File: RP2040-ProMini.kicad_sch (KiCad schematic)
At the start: 34 parts, among them J1 CONN_L, J2 CONN_U, J3 CONN_R2, J4 CONN_R, Q1 AO3400A, U1 W25Q128JVS, U2 RP2040, U3 MIC5205-3.3YM5, U4 W25Q128JVEIQ, Y1 12MHz

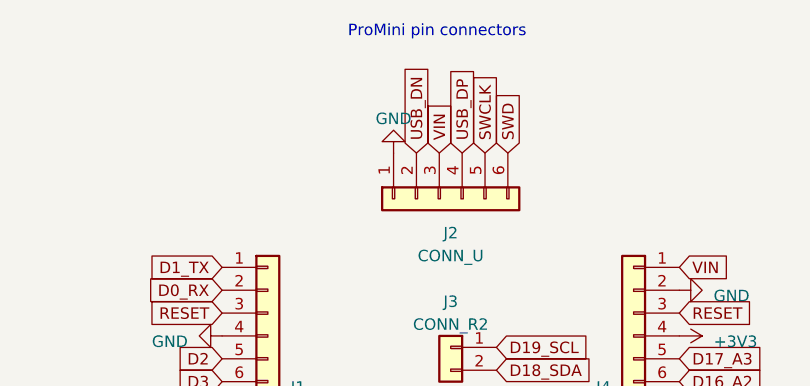
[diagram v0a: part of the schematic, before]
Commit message: Switched D- and GND on debug connector. Added missing VIN text.
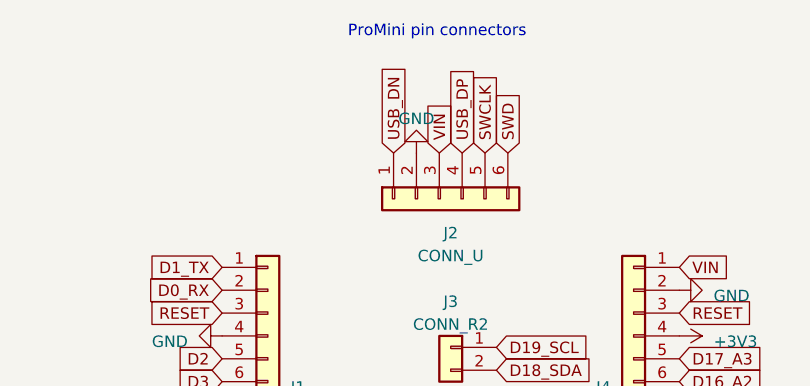
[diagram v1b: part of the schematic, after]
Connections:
- net GND: now also J2.2 (Pin_2); no longer J2.1 (Pin_1)
- net USB_DN: now also J2.1 (Pin_1); no longer J2.2 (Pin_2)
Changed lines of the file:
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@@
   (title_block
     (title "RP2040-ProMini-0010")
-    (date "2023-06-13")
+    (date "2023-06-22")
     (rev "1.0")
     (company "(c) 2023 Andriy Golovnya")
@@
     )
   )
-  (global_label "USB_DN" (shape input) (at 224.79 43.18 90) (fields_autoplaced)
-    (effects (font (size 1.27 1.27)) (justify left))
-    (property "Intersheetrefs" "${INTERSHEET_REFS}" (at 224.79 32.8961 90)
+  (global_label "USB_DN" (shape input) (at 222.25 43.18 90) (fields_autoplaced)
+    (effects (font (size 1.27 1.27)) (justify left))
+    (property "Intersheetrefs" "${INTERSHEET_REFS}" (at 222.25 32.8961 90)
       (effects (font (size 1.27 1.27)) (justify left) hide)
     )
@@
     )
   )
-  (symbol (lib_id "power:GND") (at 222.25 43.18 180) (unit 1)
-    (in_bom yes) (on_board yes) (dnp no) (fields_autoplaced)
-    (property "Reference" "#PWR037" (at 222.25 36.83 0)
-      (effects (font (size 1.27 1.27)) hide)
-    )
-    (property "Value" "GND" (at 222.25 39.37 0)
-      (effects (font (size 1.27 1.27)))
-    )
-    (property "Footprint" "" (at 222.25 43.18 0)
-      (effects (font (size 1.27 1.27)) hide)
-    )
-    (property "Datasheet" "" (at 222.25 43.18 0)
-      (effects (font (size 1.27 1.27)) hide)
-    )
+  (symbol (lib_id "power:GND") (at 224.79 43.18 180) (unit 1)
+    (in_bom yes) (on_board yes) (dnp no) (fields_autoplaced)
+    (property "Reference" "#PWR037" (at 224.79 36.83 0)
+      (effects (font (size 1.27 1.27)) hide)
+    )
+    (property "Value" "GND" (at 224.79 39.37 0)
+      (effects (font (size 1.27 1.27)))
+    )
+    (property "Footprint" "" (at 224.79 43.18 0)
+      (effects (font (size 1.27 1.27)) hide)
+    )
+    (property "Datasheet" "" (at 224.79 43.18 0)
+      (effects (font (size 1.27 1.27)) hide)
+    )

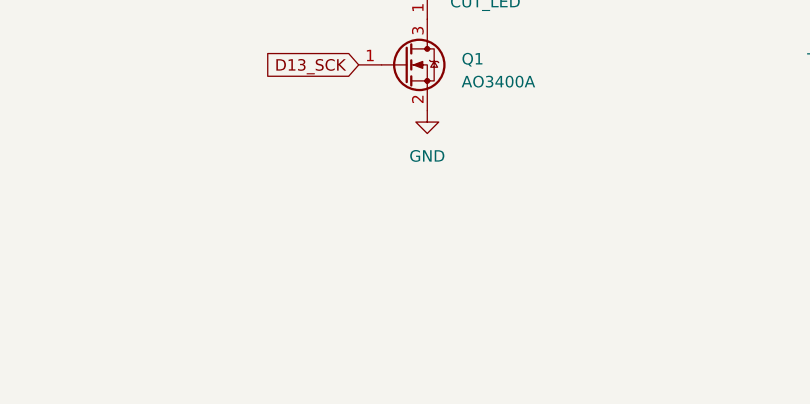
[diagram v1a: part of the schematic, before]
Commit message: Added BOOTSEL button for user convenience
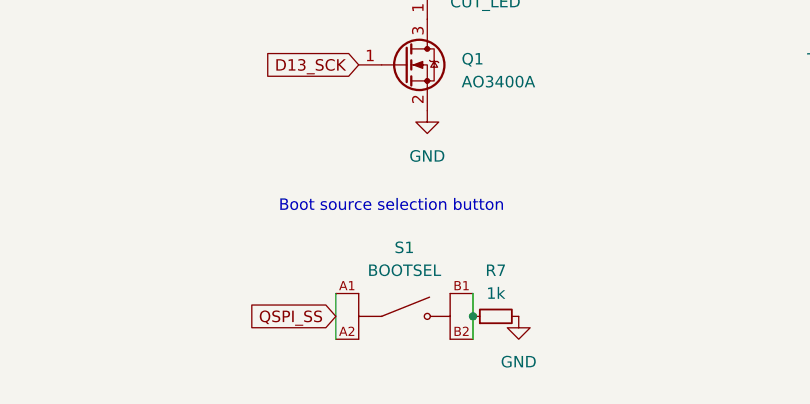
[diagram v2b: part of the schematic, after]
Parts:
- added R7: 1k, Resistor_SMD:R_0402_1005Metric, symbol Device:R_Small
- added S1: BOOTSEL, RP2040-ProMini:SW_EVPBB0AAB000, symbol EVPBB0AAB000:EVPBB0AAB000
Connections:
- net GND: now also R7.2
- net QSPI_SS: now also S1.A1, S1.A2
- new net: R7.1, S1.B1, S1.B2
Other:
- note added: "Boot source selection button"
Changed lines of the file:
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@@
   (title_block
     (title "RP2040-ProMini-0010")
-    (date "2023-06-22")
+    (date "2023-07-04")
     (rev "1.0")
     (company "(c) 2023 Andriy Golovnya")
@@
   )
   (junction (at 255.27 129.54) (diameter 0) (color 0 0 0 0)
+  )
+  (junction (at 72.39 171.45) (diameter 0) (color 0 0 0 0)
   )
   (junction (at 146.05 39.37) (diameter 0) (color 0 0 0 0)
@@
     (stroke (width 0) (type default))
   )
+  (wire (pts (xy 57.15 168.91) (xy 57.15 173.99))
+    (stroke (width 0) (type default))
+  )
   (wire (pts (xy 135.89 39.37) (xy 138.43 39.37))
     (stroke (width 0) (type default))
@@
     (stroke (width 0) (type default))
   )
+  (wire (pts (xy 72.39 171.45) (xy 72.39 173.99))
+    (stroke (width 0) (type default))
+  )
+  (wire (pts (xy 72.39 168.91) (xy 72.39 171.45))
+    (stroke (width 0) (type default))
+  )
   (wire (pts (xy 251.46 129.54) (xy 255.27 129.54))
     (stroke (width 0) (type default))
@@
     (effects (font (size 1.27 1.27)) (justify left bottom))
   )
+  (text "Boot source selection button" (at 50.8 160.02 0)
+    (effects (font (size 1.27 1.27)) (justify left bottom))
+  )
   (text "LDO power supply" (at 220.98 120.65 0)
     (effects (font (size 1.27 1.27)) (justify left bottom))
@@
     )
   )
+  (global_label "QSPI_SS" (shape input) (at 57.15 171.45 180) (fields_autoplaced)
+    (effects (font (size 1.27 1.27)) (justify right))
+    (property "Intersheetrefs" "${INTERSHEET_REFS}" (at 46.4428 171.45 0)
+      (effects (font (size 1.27 1.27)) (justify right) hide)
+    )
+  )
   (global_label "SWCLK" (shape input) (at 208.28 101.6 270) (fields_autoplaced)
     (effects (font (size 1.27 1.27)) (justify right))
@@
     )
   )
+  (symbol (lib_id "EVPBB0AAB000:EVPBB0AAB000") (at 64.77 171.45 0) (unit 1)
+    (in_bom yes) (on_board yes) (dnp no) (fields_autoplaced)
+    (property "Reference" "S1" (at 64.77 163.83 0)
+      (effects (font (size 1.27 1.27)))
+    )
+    (property "Value" "BOOTSEL" (at 64.77 166.37 0)
+      (effects (font (size 1.27 1.27)))
+    )
+    (property "Footprint" "RP2040-ProMini:SW_EVPBB0AAB000" (at 64.77 171.45 0)
+      (effects (font (size 1.27 1.27)) (justify bottom) hide)
+    )
+    (property "Datasheet" "" (at 64.77 171.45 0)
+      (effects (font (size 1.27 1.27)) hide)
+    )
+    (property "ARROW_ELECTRONICS-PURCHASE-URL" "https://snapeda.com/shop?store=Arrow+Electronics&id=584571" (at 64.77 171.45 0)
+      (effects (font (size 1.27 1.27)) (justify bottom) hide)
+    )
+    (property "MOUSER-PURCHASE-URL" "https://snapeda.com/shop?store=Mouser&id=584571" (at 64.77 171.45 0)
+      (effects (font (size 1.27 1.27)) (justify bottom) hide)
+    )
+    (property "MAXIMUM_PACKAGE_HEIGHT" "0.58mm" (at 64.77 171.45 0)
+      (effects (font (size 1.27 1.27)) (justify bottom) hide)
+    )
+    (property "PACKAGE" "None" (at 64.77 171.45 0)
+      (effects (font (size 1.27 1.27)) (justify bottom) hide)
+    )
+    (property "MF" "Panasonic Electronic" (at 64.77 171.45 0)
+      (effects (font (size 1.27 1.27)) (justify bottom) hide)
+    )
+    (property "MP" "EVPBB0AAB000" (at 64.77 171.45 0)
+      (effects (font (size 1.27 1.27)) (justify bottom) hide)
+    )
+    (property "DIGIKEY-PURCHASE-URL" "https://snapeda.com/shop?store=DigiKey&id=584571" (at 64.77 171.45 0)
+      (effects (font (size 1.27 1.27)) (justify bottom) hide)
+    )
+    (property "DIGI-KEY_PART_NUMBER" "P19888CT-ND" (at 64.77 171.45 0)
+      (effects (font (size 1.27 1.27)) (justify bottom) hide)
+    )
+    (property "DESCRIPTION" "Tactile Switch SPST-NO Top Actuated Surface Mount" (at 64.77 171.45 0)
+      (effects (font (size 1.27 1.27)) (justify bottom) hide)
+    )
+    (pin "A1")
+    (pin "A2")
+    (pin "B1")
+    (pin "B2")
+    (instances
+      (project "RP2040-ProMini"
+        (path "/9a38a81c-7302-494f-9784-2ab4342a0a1d"
+          (reference "S1") (unit 1)
+        )
+      )
+    )
+  )
   (symbol (lib_id "Device:C_Small") (at 248.92 99.06 0) (unit 1)
     (in_bom yes) (on_board yes) (dnp no) (fields_autoplaced)
@@
         (path "/9a38a81c-7302-494f-9784-2ab4342a0a1d"
           (reference "#PWR09") (unit 1)
+        )
+      )
+    )
+  )
+  (symbol (lib_id "power:GND") (at 77.47 171.45 0) (unit 1)
+    (in_bom yes) (on_board yes) (dnp no) (fields_autoplaced)
+    (property "Reference" "#PWR049" (at 77.47 177.8 0)
+      (effects (font (size 1.27 1.27)) hide)
+    )
+    (property "Value" "GND" (at 77.47 176.53 0)
+      (effects (font (size 1.27 1.27)))
+    )
+    (property "Footprint" "" (at 77.47 171.45 0)
+      (effects (font (size 1.27 1.27)) hide)
+    )
+    (property "Datasheet" "" (at 77.47 171.45 0)
+      (effects (font (size 1.27 1.27)) hide)
+    )
+    (pin "1")
+    (instances
+      (project "RP2040-ProMini"
+        (path "/9a38a81c-7302-494f-9784-2ab4342a0a1d"
+          (reference "#PWR049") (unit 1)
         )
       )
@@
         )
       )
+    )
+  )
+  (symbol (lib_id "Device:R_Small") (at 74.93 171.45 90) (unit 1)
+    (in_bom yes) (on_board yes) (dnp no) (fields_autoplaced)
+    (property "Reference" "R7" (at 74.93 166.37 90)
+      (effects (font (size 1.27 1.27)))
+    )
+    (property "Value" "1k" (at 74.93 168.91 90)
+      (effects (font (size 1.27 1.27)))
+    )
+    (property "Footprint" "Resistor_SMD:R_0402_1005Metric" (at 74.93 171.45 0)
+      (effects (font (size 1.27 1.27)) hide)
+    )
+    (property "Datasheet" "~" (at 74.93 171.45 0)
+      (effects (font (size 1.27 1.27)) hide)
+    )
+    (pin "1")
+    (pin "2")
+    (instances
+      (project "RP2040-ProMini"
+        (path "/9a38a81c-7302-494f-9784-2ab4342a0a1d"
+          (reference "R7") (unit 1)
+        )
+      )

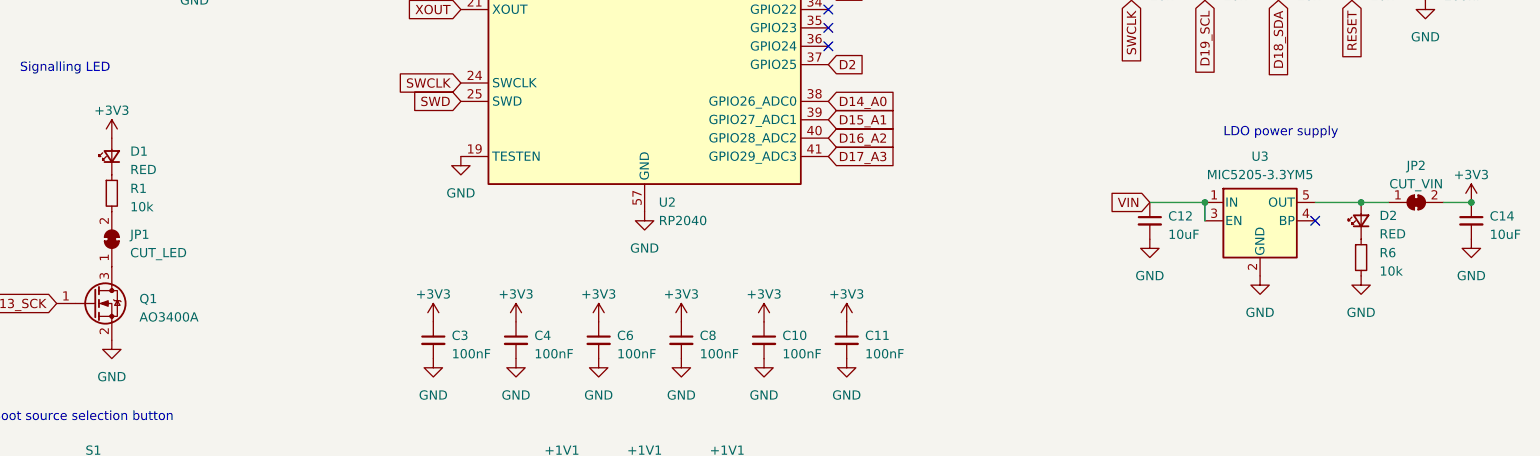
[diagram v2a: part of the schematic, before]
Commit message: Spin off v1.1 to reflect new BOOTSEL button.
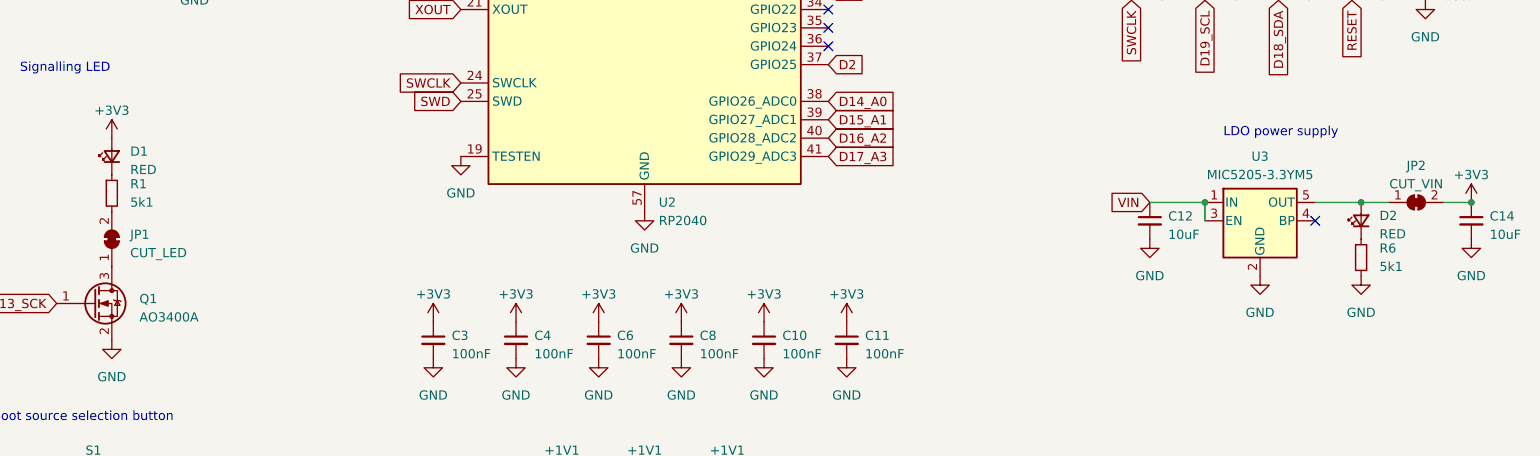
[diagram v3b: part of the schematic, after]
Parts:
- R1, R6: value 10k -> 5k1
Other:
- title: RP2040-ProMini-0010 -> RP2040-ProMini-0011
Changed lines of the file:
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@@
   (paper "A4")
   (title_block
-    (title "RP2040-ProMini-0010")
-    (date "2023-07-04")
-    (rev "1.0")
+    (title "RP2040-ProMini-0011")
+    (date "2023-07-05")
+    (rev "1.1")
     (company "(c) 2023 Andriy Golovnya")
     (comment 1 "RP2040 based board with Arduino Pro Mini footprint")
@@
   (symbol (lib_id "Device:R_Small") (at 67.31 128.27 0) (unit 1)
     (in_bom yes) (on_board yes) (dnp no) (fields_autoplaced)
-    (property "Reference" "R1" (at 69.85 127.635 0)
-      (effects (font (size 1.27 1.27)) (justify left))
-    )
-    (property "Value" "10k" (at 69.85 130.175 0)
+    (property "Reference" "R1" (at 69.85 127 0)
+      (effects (font (size 1.27 1.27)) (justify left))
+    )
+    (property "Value" "5k1" (at 69.85 129.54 0)
       (effects (font (size 1.27 1.27)) (justify left))
     )
@@
   (symbol (lib_id "Device:R_Small") (at 240.03 137.16 0) (unit 1)
     (in_bom yes) (on_board yes) (dnp no) (fields_autoplaced)
-    (property "Reference" "R6" (at 242.57 136.525 0)
-      (effects (font (size 1.27 1.27)) (justify left))
-    )
-    (property "Value" "10k" (at 242.57 139.065 0)
-      (effects (font (size 1.27 1.27)) (justify left))
-    )
+    (property "Reference" "R6" (at 242.57 135.89 0)
+      (effects (font (size 1.27 1.27)) (justify left))
+    )
+    (property "Value" "5k1" (at 242.57 138.43 0)
+      (effects (font (size 1.27 1.27)) (justify left))
+    )

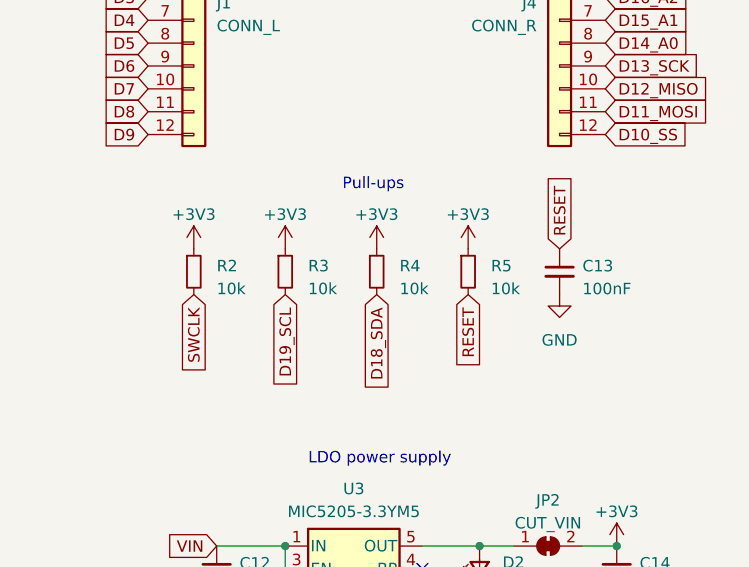
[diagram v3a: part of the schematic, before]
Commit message: Removed pull-up resistor for SWDCLK line.
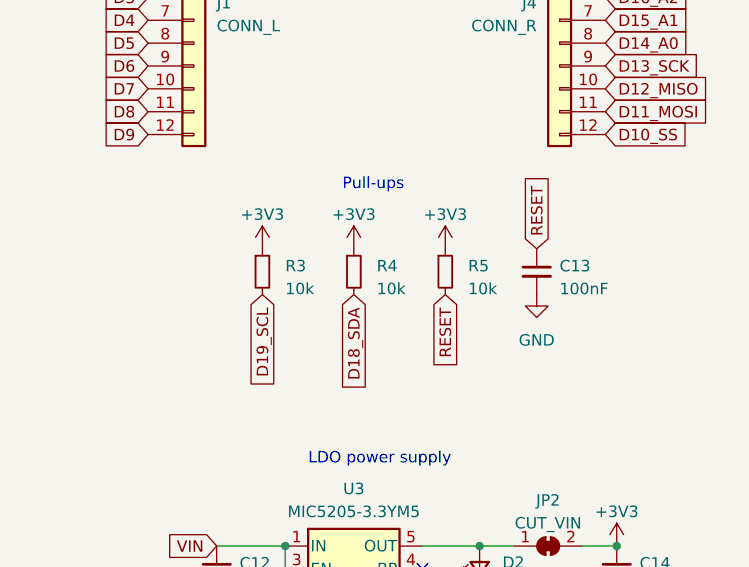
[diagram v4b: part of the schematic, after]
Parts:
- removed R2: 10k, Resistor_SMD:R_0402_1005Metric, symbol Device:R_Small
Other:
- moved on the sheet: C13, R3, R4, R5

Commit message: Increased board version
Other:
- title: RP2040-ProMini-0011 -> RP2040-ProMini-0012
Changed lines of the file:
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@@
   (paper "A4")
   (title_block
-    (title "RP2040-ProMini-0011")
+    (title "RP2040-ProMini-0012")
     (date "2023-11-21")
-    (rev "1.1")
+    (rev "1.2")
     (company "(c) 2023 Andriy Golovnya")
     (comment 1 "RP2040 based board with Arduino Pro Mini footprint")

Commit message: Changed board version to 1.3.
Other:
- company: (c) 2023 Andriy Golovnya -> (c) 2023-2024 Andriy Golovnya
- title: RP2040-ProMini-0012 -> RP2040-ProMini-0013
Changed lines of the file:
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@@
   (paper "A4")
   (title_block
-    (title "RP2040-ProMini-0012")
-    (date "2023-11-21")
-    (rev "1.2")
-    (company "(c) 2023 Andriy Golovnya")
+    (title "RP2040-ProMini-0013")
+    (date "2024-01-01")
+    (rev "1.3")
+    (company "(c) 2023-2024 Andriy Golovnya")
     (comment 1 "RP2040 based board with Arduino Pro Mini footprint")
   )
